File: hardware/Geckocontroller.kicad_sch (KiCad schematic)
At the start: 114 parts, among them J1 SHT31, J101 AC Input, J11 RGB LED, J21 BME280, J31 DS18B20 I, J32 DS18B20 II, J40 FAN, J50 USB-C, J51 UART, J60 Load Cell Connector, J70 SPI / Addon Connector, J81 Dimmer, J91 Pump, J92 HeatBed, J93 HeatLamp, K81 AQG12212, K91 AQG12112, K92 AQG12112, K93 AQG12112, Q11 AO3400A, Q12 AO3400A, Q13 AO3400A, Q40 AO3400A, Q41 AO3401A, Q51 S8050, Q52 S8050, Q61 S8550, Q81 AO3400A, Q91 AO3400A, Q92 AO3400A, Q93 AO3400A, SW1 Boot, SW2 Reset, U1 ESP32-WROOM-32, U101 ACT4088, U2 CP2102, U61 HX711, U81 6N138

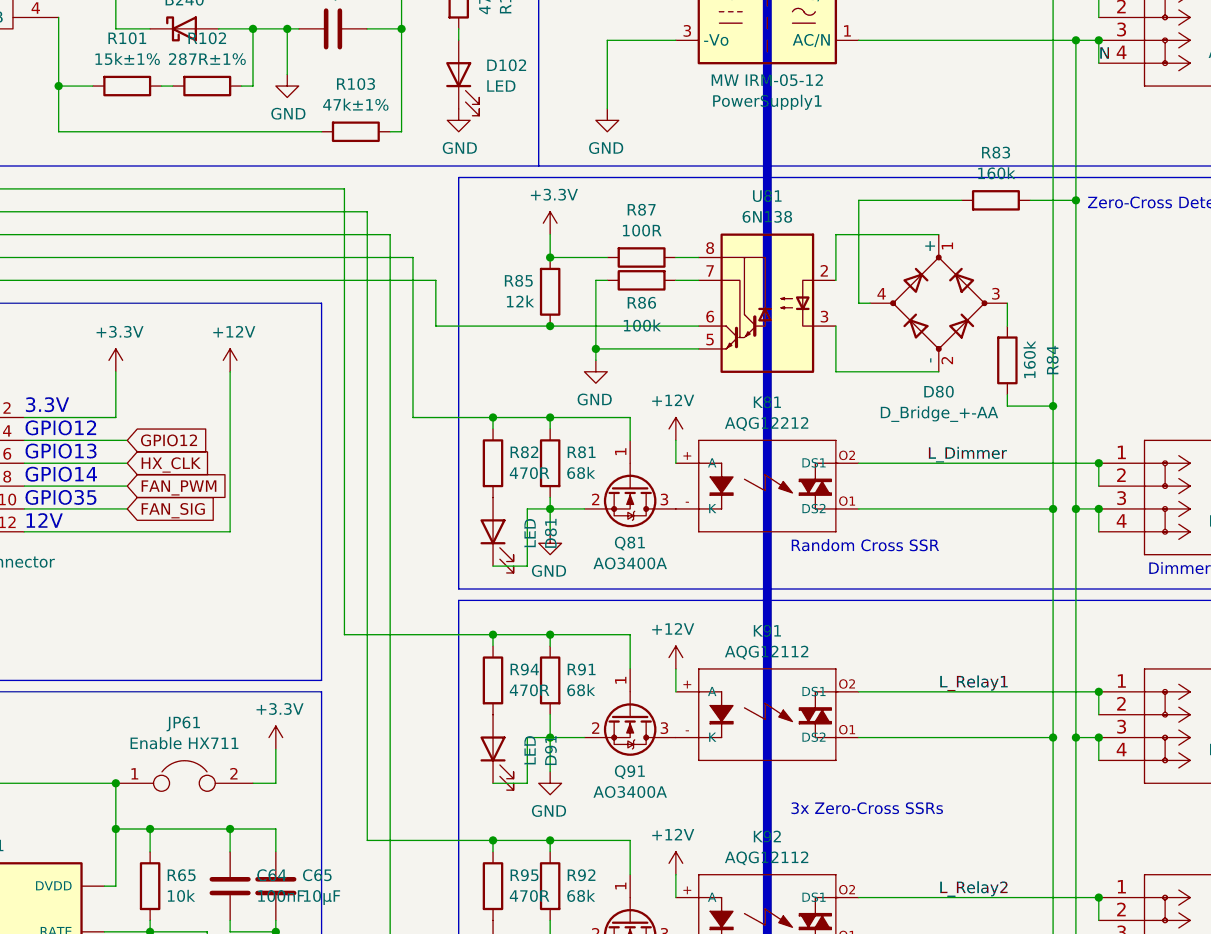
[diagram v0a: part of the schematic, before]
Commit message: Hardware (Schema+PCB): Change ZC Resistors
* use 1206 instead of 0805 footprints
* explicitely rate 400V+
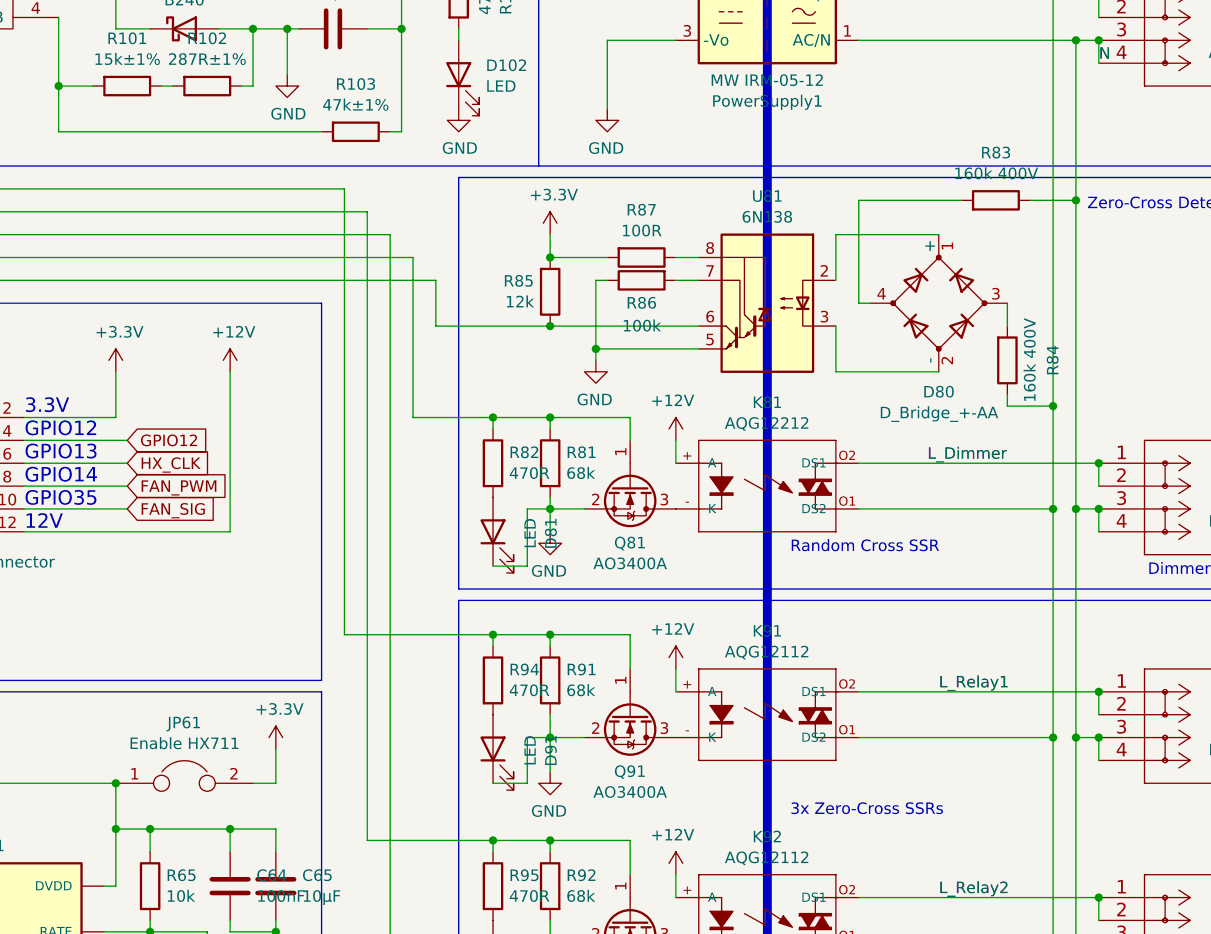
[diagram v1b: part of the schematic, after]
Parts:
- R83, R84: value 160k -> 160k 400V; footprint Resistor_SMD:R_0805_2012Metric_Pad1.20x1.40mm_HandSolder -> Resistor_SMD:R_1206_3216Metric_Pad1.30x1.75mm_HandSolder
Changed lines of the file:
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@@
     (in_bom yes) (on_board yes)
     (property "Reference" "R83" (id 0) (at 313.69 45.5422 90))
-    (property "Value" "160k" (id 1) (at 313.69 47.8536 90))
-    (property "Footprint" "Resistor_SMD:R_0805_2012Metric_Pad1.20x1.40mm_HandSolder" (id 2) (at 313.69 52.578 90)
+    (property "Value" "160k 400V" (id 1) (at 313.69 47.8536 90))
+    (property "Footprint" "Resistor_SMD:R_1206_3216Metric_Pad1.30x1.75mm_HandSolder" (id 2) (at 313.69 52.578 90)
       (effects (font (size 1.27 1.27)) hide)
     )
@@
     (in_bom yes) (on_board yes)
     (property "Reference" "R84" (id 0) (at 320.04 68.58 90))
-    (property "Value" "160k" (id 1) (at 317.5 68.58 90))
-    (property "Footprint" "Resistor_SMD:R_0805_2012Metric_Pad1.20x1.40mm_HandSolder" (id 2) (at 313.182 68.58 90)
+    (property "Value" "160k 400V" (id 1) (at 317.5 68.58 90))
+    (property "Footprint" "Resistor_SMD:R_1206_3216Metric_Pad1.30x1.75mm_HandSolder" (id 2) (at 313.182 68.58 90)
       (effects (font (size 1.27 1.27)) hide)
     )
@@
     )
     (path "/00000000-0000-0000-0000-000060221a24"
-      (reference "R83") (unit 1) (value "160k") (footprint "Resistor_SMD:R_0805_2012Metric_Pad1.20x1.40mm_HandSolder")
+      (reference "R83") (unit 1) (value "160k 400V") (footprint "Resistor_SMD:R_1206_3216Metric_Pad1.30x1.75mm_HandSolder")
     )
     (path "/00000000-0000-0000-0000-00006093c1b0"
-      (reference "R84") (unit 1) (value "160k") (footprint "Resistor_SMD:R_0805_2012Metric_Pad1.20x1.40mm_HandSolder")
+      (reference "R84") (unit 1) (value "160k 400V") (footprint "Resistor_SMD:R_1206_3216Metric_Pad1.30x1.75mm_HandSolder")
     )
     (path "/00000000-0000-0000-0000-0000611ea8b9"
